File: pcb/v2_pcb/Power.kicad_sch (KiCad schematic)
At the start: 0 parts

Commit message: sdf
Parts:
- added BT1: Battery, symbol Device:Battery
- added C10, C42, C56, C62, C81, C82, C84, C85, C87, C88, C9, C91: 10uF, symbol Device:C_Small
- added C11, C83, C86: 100nF, symbol Device:C_Small
- added C49, C53: 47nF, 10v+ ceram, symbol Device:C_Small
- added C92: 4.7uF, symbol Device:C_Small
- added D2: LED, symbol Device:LED
- added L1: L, symbol Device:L
- added Q3: NMOS, symbol Simulation_SPICE:NMOS
- added R23: 100, symbol Device:R_Small_US
- added R24, R26, R29, R30, R31: 10k, symbol Device:R_Small_US
- added R25: 8.2k, symbol Device:R_Small_US
- added R28: 2k2, symbol Device:R_Small_US
- added TP1: TestPoint_Small, symbol Connector:TestPoint_Small
- added U6: BQ25798RQMR, BQ25798RQMR:IC_BQ25798RQMR, symbol noob:BQ25798RQMR
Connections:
- new net: C56.2, C62.2, C81.2, C82.2, C83.2, U6.25 (SYS)
- new net: C49.1, L1.1, U6.28 (SW1)
- new net: C53.1, L1.2, U6.26 (SW2)
- new net: C10.2, C11.2, C42.2, C9.2, U6.10 (ACDRV2), U6.11 (ACDRV1), U6.2 (VBUS), U6.3 (VBUS)
- new net: R25.2, R26.2, U6.16 (TS)
- new net: R28.1, U6.1 (STAT)
- new net: D2.1 (K), R28.2
- new net: R23.1, U6.18 (BATP)
- new net: C86.2, C87.2, C88.2, C91.2, U6.29 (PMID)
- new net: TP1.1, U6.12 (~{QON})
- new net: C53.2, U6.19 (BTST2)
- new net: Q3.2 (G), U6.24 (SDRV)
- new net: C49.2, U6.4 (BTST1)
- new net +3V3: D2.2 (A), R29.2, R30.2, R31.2
- new net BAT: C84.1, C85.1, Q3.3 (S), U6.22 (BAT), U6.23 (BAT)
- new net CHG_INT: R31.1, U6.21 (~{INT})
- new net CHG_SCL: R30.1, U6.14 (SCL)
- new net CHG_SDA: R29.1, U6.15 (SDA)
- new net GND: C10.1, C11.1, C42.1, C56.1, C62.1, C81.1, C82.1, C83.1, C84.2, C85.2, C86.1, C87.1, C88.1, C9.1, C91.1, C92.1, R24.2, R26.1, U6.13 (~{CE}), U6.17 (ILIM_HIZ), U6.20 (PROG), U6.27 (GND), U6.8 (VAC2), U6.9 (VAC1)
- new net REGN: C92.2, R24.1, R25.1, U6.5 (REGN)
- new net vpack+: Q3.1 (D), R23.2
- no-connect marks 0 -> 2

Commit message: finish battery charger
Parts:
- removed BT1: Battery, symbol Device:Battery
- added R35: 8.2k, symbol Device:R_Small_US
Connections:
- net GND: now also R35.1; no longer U6.20 (PROG)
- new net: R35.2, U6.20 (PROG)
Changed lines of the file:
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@@
 	(wire
 		(pts
-			(xy 128.27 92.71) (xy 144.78 92.71)
+			(xy 128.27 92.71) (xy 132.08 92.71)
 		)
 		(stroke
@@
 	(wire
 		(pts
+			(xy 137.16 92.71) (xy 144.78 92.71)
+		)
+		(stroke
+			(width 0)
+			(type default)
+		)
+	)
+	(wire
+		(pts
 			(xy 48.26 114.3) (xy 66.04 114.3)
 		)
@@
 	(wire
 		(pts
-			(xy 162.56 71.12) (xy 180.34 71.12)
+			(xy 162.56 71.12) (xy 218.44 71.12)
 		)
 		(stroke
@@
 		(pts
 			(xy 148.59 83.82) (xy 157.48 83.82)
+		)
+		(stroke
+			(width 0)
+			(type default)
+		)
+	)
+	(wire
+		(pts
+			(xy 218.44 71.12) (xy 218.44 152.4)
 		)
 		(stroke
@@
 	)
 	(symbol
+		(lib_id "Device:R_Small_US")
+		(at 134.62 92.71 270)
+		(unit 1)
+		(body_style 1)
+		(exclude_from_sim no)
+		(in_bom yes)
+		(on_board yes)
+		(in_pos_files yes)
+		(dnp no)
+		(property "Reference" "R35"
+			(at 131.318 90.932 90)
+			(show_name no)
+			(do_not_autoplace no)
+			(effects
+				(font
+					(size 1.27 1.27)
+				)
+			)
+		)
+		(property "Value" "8.2k"
+			(at 138.43 90.932 90)
+			(show_name no)
+			(do_not_autoplace no)
+			(effects
+				(font
+					(size 1.27 1.27)
+				)
+			)
+		)
+		(property "Footprint" ""
+			(at 134.62 92.71 0)
+			(hide yes)
+			(show_name no)
+			(do_not_autoplace no)
+			(effects
+				(font
+					(size 1.27 1.27)
+				)
+			)
+		)
+		(property "Datasheet" ""
+			(at 134.62 92.71 0)
+			(hide yes)
+			(show_name no)
+			(do_not_autoplace no)
+			(effects
+				(font
+					(size 1.27 1.27)
+				)
+			)
+		)
+		(property "Description" "Resistor, small US symbol"
+			(at 134.62 92.71 0)
+			(hide yes)
+			(show_name no)
+			(do_not_autoplace no)
+			(effects
+				(font
+					(size 1.27 1.27)
+				)
+			)
+		)
+		(pin "2"
+		)
+		(pin "1"
+		)
+		(instances
+			(project "open-race_v2"
+				(path "/1cc14db4-4207-4c76-b5f6-6a2491c5fa6b/f75a094f-afff-47fb-af28-3f9eed6a2864"
+					(reference "R35")
+					(unit 1)
+				)
+			)
+		)
+	)
+	(symbol
 		(lib_id "Device:C_Small")
 		(at 50.8 66.04 0)
@@
 					(unit 1)
 				)
-			)
-		)
-	)
-	(symbol
-		(lib_id "Device:Battery")
-		(at 198.12 40.64 0)
-		(unit 1)
-		(body_style 1)
-		(exclude_from_sim no)
-		(in_bom yes)
-		(on_board yes)
-		(in_pos_files yes)
-		(dnp no)
-		(fields_autoplaced yes)
-		(property "Reference" "BT1"
-			(at 201.93 38.7984 0)
-			(show_name no)
-			(do_not_autoplace no)
-			(effects
-				(font
-					(size 1.27 1.27)
-				)
-				(justify left)
-			)
-		)
-		(property "Value" "Battery"
-			(at 201.93 41.3384 0)
-			(show_name no)
-			(do_not_autoplace no)
-			(effects
-				(font
-					(size 1.27 1.27)
-				)
-				(justify left)
-			)
-		)
-		(property "Footprint" ""
-			(at 198.12 39.116 90)
-			(hide yes)
-			(show_name no)
-			(do_not_autoplace no)
-			(effects
-				(font
-					(size 1.27 1.27)
-				)
-			)
-		)
-		(property "Datasheet" ""
-			(at 198.12 39.116 90)
-			(hide yes)
-			(show_name no)
-			(do_not_autoplace no)
-			(effects
-				(font
-					(size 1.27 1.27)
-				)
-			)
-		)
-		(property "Description" "Multiple-cell battery"
-			(at 198.12 40.64 0)
-			(hide yes)
-			(show_name no)
-			(do_not_autoplace no)
-			(effects
-				(font
-					(size 1.27 1.27)
-				)
-			)
-		)
-		(property "Sim.Device" "V"
-			(at 198.12 40.64 0)
-			(hide yes)
-			(show_name no)
-			(do_not_autoplace no)
-			(effects
-				(font
-					(size 1.27 1.27)
-				)
-			)
-		)
-		(property "Sim.Type" "DC"
-			(at 198.12 40.64 0)
-			(hide yes)
-			(show_name no)
-			(do_not_autoplace no)
-			(effects
-				(font
-					(size 1.27 1.27)
-				)
-			)
-		)
-		(property "Sim.Pins" "1=+ 2=-"
-			(at 198.12 40.64 0)
-			(hide yes)
-			(show_name no)
-			(do_not_autoplace no)
-			(effects
-				(font
-					(size 1.27 1.27)
-				)
-			)
-		)
-		(pin "2"
-		)
-		(pin "1"
-		)
-		(instances
-			(project "open-race_v2"
-				(path "/1cc14db4-4207-4c76-b5f6-6a2491c5fa6b/f75a094f-afff-47fb-af28-3f9eed6a2864"
-					(reference "BT1")
-					(unit 1)
-				)

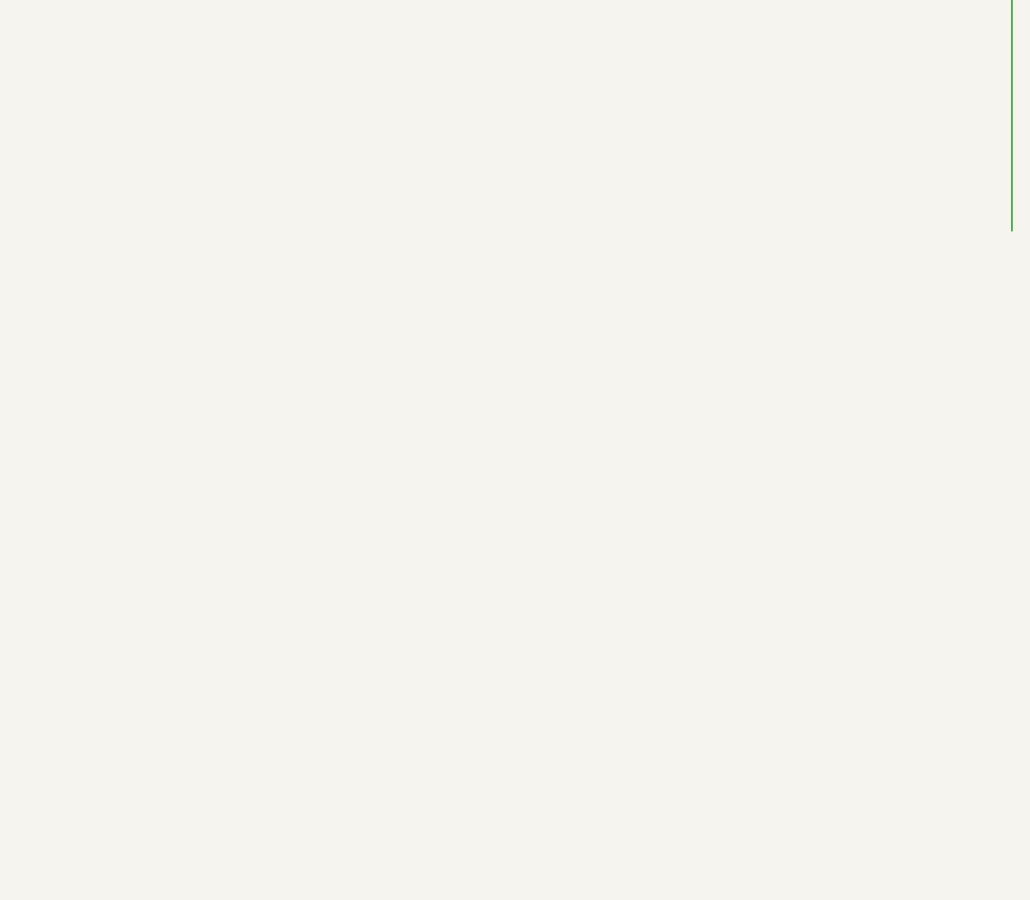
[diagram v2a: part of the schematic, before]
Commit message: start on battery safety
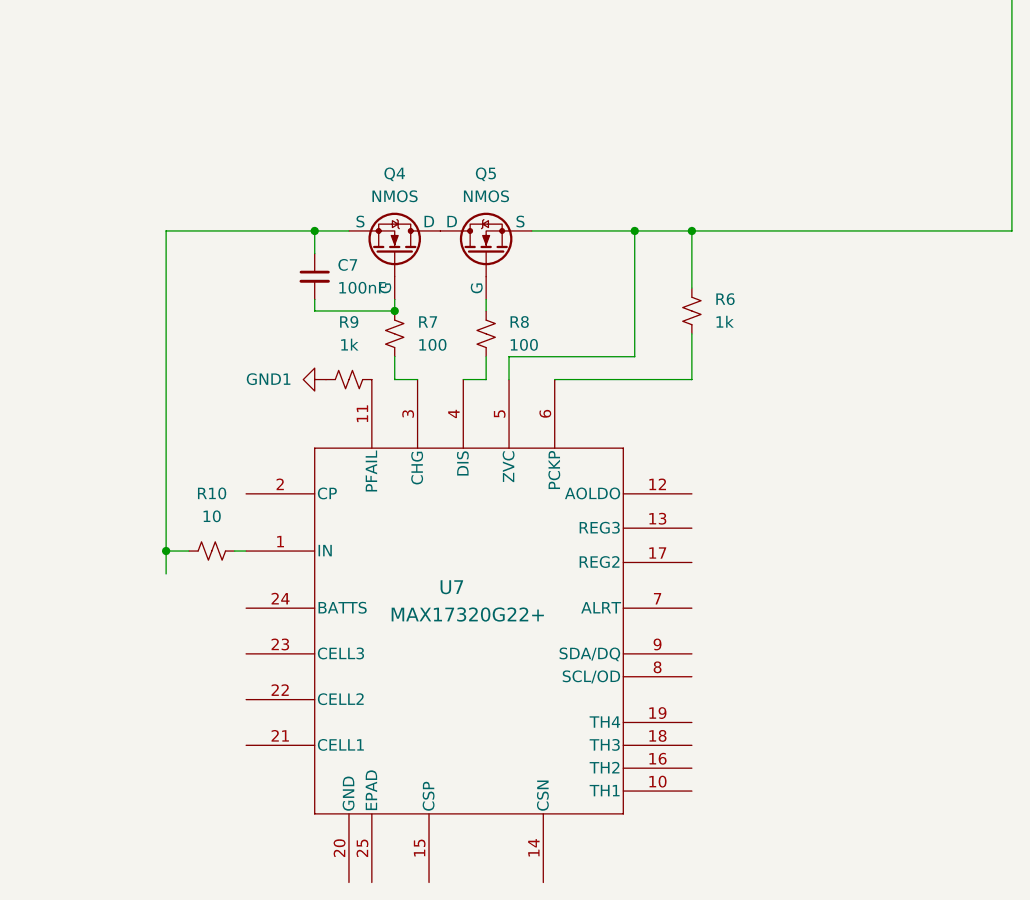
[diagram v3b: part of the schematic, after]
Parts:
- added C7: 100nF, symbol Device:C_Small
- added Q4, Q5: NMOS, symbol Simulation_SPICE:NMOS
- added R10: 10, symbol Device:R_Small_US
- added R6, R9: 1k, symbol Device:R_Small_US
- added R7, R8: 100, symbol Device:R_Small_US
- added U7: MAX17320G22+, 21-0139I_T2444-4_MXM, symbol noob:MAX17320G22+
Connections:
- net vpack+: now also Q5.3 (S), R6.1, U7.5 (ZVC)
- new net: R10.2, U7.1 (IN)
- new net: R9.2, U7.11 (PFAIL)
- new net: R7.2, U7.3 (CHG)
- new net: R8.2, U7.4 (DIS)
- new net: R6.2, U7.6 (PCKP)
- new net: Q4.1 (D), Q5.1 (D)
- new net: C7.2, Q4.2 (G), R7.1
- new net: C7.1, Q4.3 (S), R10.1
- new net: Q5.2 (G), R8.1
- new net GND1: R9.1
